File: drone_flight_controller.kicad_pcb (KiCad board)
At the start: 4 copper layers, 37 x 37 mm, 67 parts, among them J1 Conn_01x08_MountingPin, J2 USB_C_Receptacle_USB2.0_16P, U1 STM32H743VITx, U2 IST8310, U3 BMP388, U4 ICM-42688-P, U5 LT3045xDD, U6 LM5164DDA, Y1 25MHz, Y2 32.768KHz

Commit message: started placing some items
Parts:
- added H1: MountingHole, MountingHole:MountingHole_3.2mm_M3, F.Cu at (127.8, 52.8)
- added H2: MountingHole, MountingHole:MountingHole_3.2mm_M3, F.Cu at (158.2, 52.8)
- added H3: MountingHole, MountingHole:MountingHole_3.2mm_M3, F.Cu at (127.8, 83.2)
- added H4: MountingHole, MountingHole:MountingHole_3.2mm_M3, F.Cu at (158.2, 83.2)
- C10, C11, C12, C13, C14, C15, C6, C61, C62, C69, C70, C8, C9, FB1, U1, Y1, Y2: moved to B.Cu
- moved C62 87.3 mm to (151.9, 59.8), turned to -90 degrees
- moved C61 83.8 mm to (151.9, 61.6), turned to 90 degrees
- moved Y2 81.1 mm to (150.3, 60.7), turned to -90 degrees
- moved C4 74.5 mm to (201.9, 157.1)
- moved C1 74.5 mm to (217.5, 150.7)
- moved C2 74.5 mm to (216.5, 151.7)
- moved C21 74.5 mm to (247.2, 147.3)
- moved C25 74.5 mm to (206.4, 108.1)
- moved C26 74.5 mm to (206.4, 110.0)
- moved C3 74.5 mm to (214.3, 152.2)
- moved D1 74.5 mm to (202.2, 153.1)
- moved D2 74.5 mm to (202.2, 155.1)
- moved D3 74.5 mm to (247.4, 141.3)
- moved D4 74.5 mm to (247.4, 143.3)
- moved R1 74.5 mm to (199.0, 153.1)
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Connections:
- net /IMU_INT renamed /IMU_INT1
- net Net-(U2-C1) renamed /IST8310_C1
- C28 pad 1: Net-(U2-AVDD) -> +3.3V
- C29 pad 1: Net-(U2-AVDD) -> +3.3V
- U2 pad 13: Net-(U2-AVDD) -> +3.3V
- U2 pad 2: Net-(U2-AVDD) -> +3.3V
- U4 pad 9: unconnected-(U4-INT2/FSYNC/CLKIN-Pad9) -> /IMU_INT2
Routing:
- net /BUCK_SW_R: track 0.00 -> 11.0 mm, vias 0 -> 2
- net /BUCK_OUT: track 0.00 -> 7.84 mm
- net /LDO_PG: track 0.00 -> 4.15 mm, vias 0 -> 1
- net /BUCK_FB: track 0.00 -> 3.58 mm
- net /BUCK_SW: track 0.00 -> 2.79 mm
- net /LDO_IN: track 0.00 -> 2.26 mm, vias 0 -> 1
- net /BUCK_BST: track 0.00 -> 1.69 mm
- net +3.3V: track 0.00 -> 1.45 mm, vias 0 -> 3
- net /LDO_PGFB: track 0.00 -> 1.39 mm
- net /LDO_SET: track 0.00 -> 0.94 mm
- added copper zone on F.Cu, net +3.3V
- added copper zone on F.Cu, net /BUCK_OUT
- added copper zone on F.Cu, net /LDO_IN
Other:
- board size 37 x 37 mm -> 36 x 36 mm

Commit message: more placing and routing
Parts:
- R12, R13, R14, R15: moved to B.Cu
- moved R15 132.8 mm to (153.8, 69.9), turned to 90 degrees
- moved R14 132.2 mm to (153.8, 71.7), turned to 90 degrees
- moved R13 131.4 mm to (153.9, 76.2), turned to -90 degrees
- moved R12 127.5 mm to (157.8, 73.1)
- moved C1 117.1 mm to (142.4, 60.9)
- moved C2 117.1 mm to (141.4, 61.9)
- moved C3 117.1 mm to (139.2, 62.4)
- moved U4 117.1 mm to (139.7, 59.9)
- moved C4 101.4 mm to (145.8, 72.6), turned to 90 degrees
- moved D2 100.4 mm to (144.9, 72.6), turned to 90 degrees
- moved R2 99.2 mm to (144.0, 72.6), turned to 90 degrees
- moved D1 96.8 mm to (146.3, 74.0), turned to 180 degrees
- moved R1 96.1 mm to (144.4, 74.0)
- moved U3 74.1 mm to (157.6, 64.6)
- moved C26 67.4 mm to (158.4, 62.8)
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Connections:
- net Net-(J2-CC1) renamed /CC1
- net Net-(J2-CC2) renamed /CC2
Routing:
- net /MOT_1: track 0.00 -> 18.0 mm, vias 0 -> 1
- net /MOT_2: track 0.00 -> 17.4 mm, vias 0 -> 1
- net /MOT_3: track 0.00 -> 16.9 mm, vias 0 -> 1
- net /MOT_4: track 0.00 -> 15.9 mm, vias 0 -> 1
- net /VBAT_REF: track 0.00 -> 10.5 mm, vias 0 -> 1
- net /USB_VBUS: track 0.00 -> 9.03 mm
- net +3V3: track 0.00 -> 1.58 mm
- net /CC2: track 0.00 -> 1.06 mm
- net /CC1: track 0.00 -> 1.05 mm
- net /USB_VBUS_SNS: track 0.00 -> 0.86 mm
- added copper zone on F.Cu, net /VBAT_REF

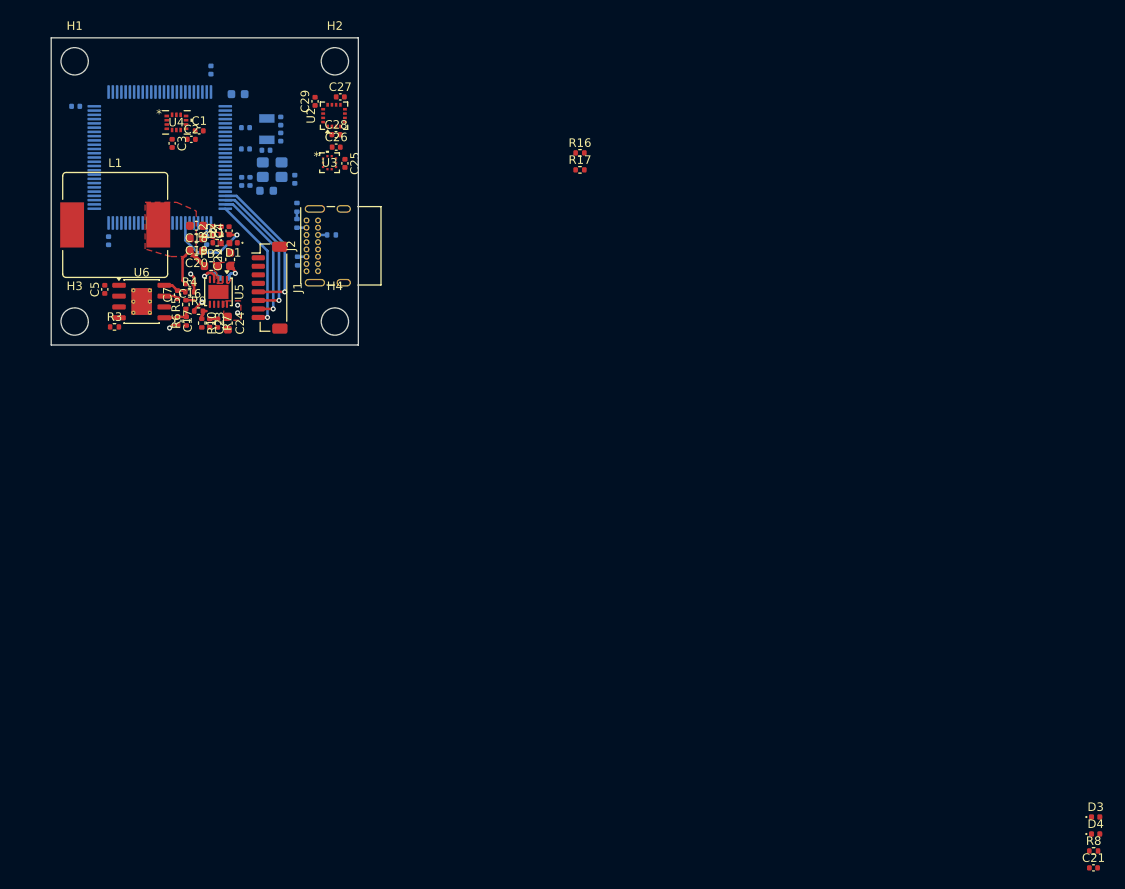
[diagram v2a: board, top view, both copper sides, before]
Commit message: added most components
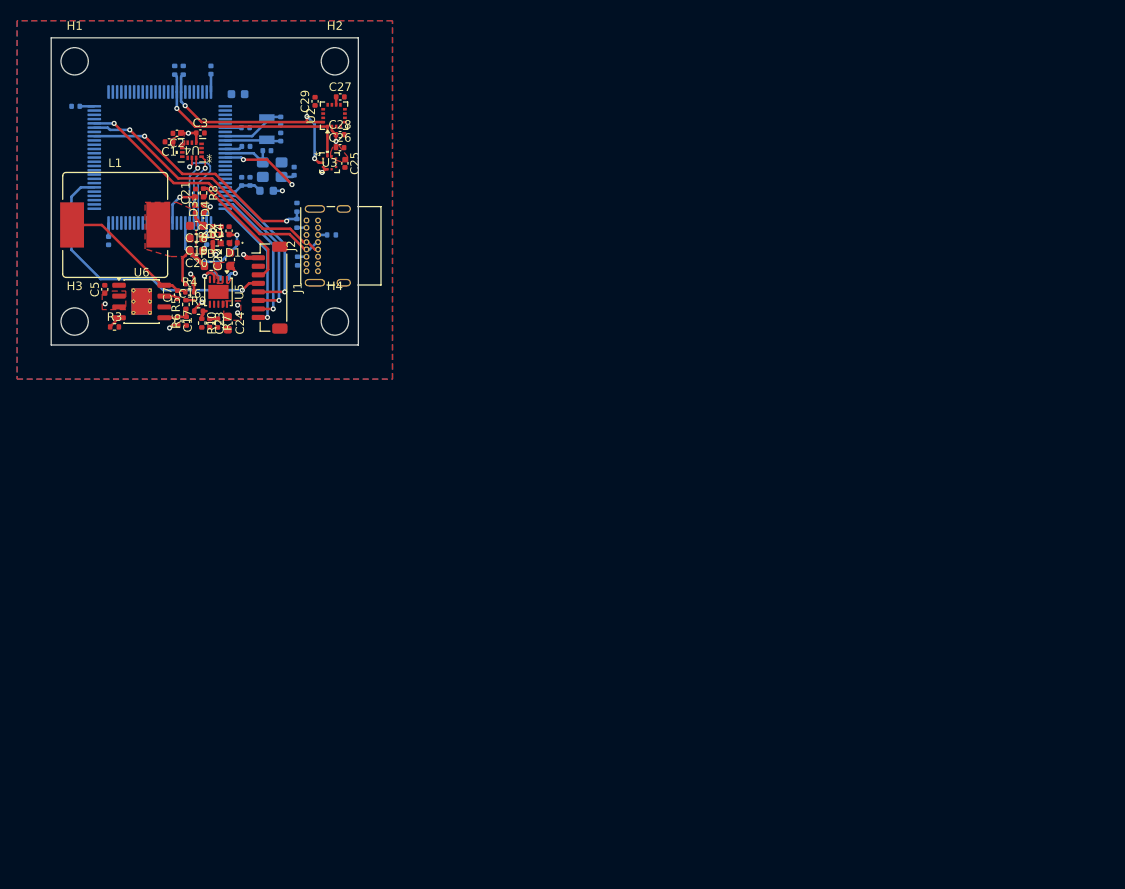
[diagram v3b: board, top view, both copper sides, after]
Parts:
- C17: value 82pF -> 56pF
- L1: value 56uH -> 33uH
- R16, R17: moved to B.Cu
- R3: value 64.9k -> 41.2k
- R4: value 422k -> 237k
- R5: value 220k -> 316k
- moved C21 131.6 mm to (141.9, 68.2), turned to 90 degrees
- moved R8 129.7 mm to (142.8, 68.2), turned to -90 degrees
- moved D4 128.5 mm to (141.9, 70.1), turned to -90 degrees
- moved D3 126.6 mm to (142.8, 70.0), turned to 90 degrees
- moved R16 48.5 mm to (139.5, 53.8), turned to -90 degrees
- moved R17 47.9 mm to (140.5, 53.8), turned to -90 degrees
- moved C69 4.68 mm to (150.3, 63.2), turned to 0 degrees
- moved C70 4.11 mm to (153.5, 65.6), turned to 90 degrees
- moved C1 3.76 mm to (138.8, 62.2), turned to 180 degrees
- moved U4 3.74 mm to (141.5, 63.2), turned to 180 degrees
- moved C3 3.52 mm to (142.5, 61.1), turned to 0 degrees
- moved C2 1.82 mm to (139.7, 61.2), turned to 180 degrees
- moved C28 0.47 mm to (158.8, 61.3)
- moved C26 0.45 mm to (158.8, 62.9)
- moved C15 0.30 mm to (147.8, 62.7)
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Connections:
- net /BUCK_OUT renamed +5V
- C10 pad 1: +3V3 -> +3.3V
- C11 pad 1: +3V3 -> +3.3V
- C12 pad 1: +3V3 -> +3.3V
- C15 pad 1: +3V3 -> +3.3V
- C6 pad 1: +3V3 -> +3.3V
- C8 pad 1: +3V3 -> +3.3V
- C9 pad 1: +3V3 -> +3.3V
- FB1 pad 2: +3V3 -> +3.3V
- U1 pad 100: +3V3 -> +3.3V
- U1 pad 11: +3V3 -> +3.3V
- U1 pad 27: +3V3 -> +3.3V
- U1 pad 28: /SPI_CS -> unconnected-(U1-PA4-Pad28)
- U1 pad 50: +3V3 -> +3.3V
- U1 pad 6: +3V3 -> +3.3V
- U1 pad 75: +3V3 -> +3.3V
- U1 pad 92: unconnected-(U1-PB6-Pad92) -> /I2C_SCL
- U1 pad 93: unconnected-(U1-PB7-Pad93) -> /I2C_SDA
- U4 pad 12: /SPI_CS -> /IMU_CS
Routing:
- net /ESC_TELEM: track 0.00 -> 33.5 mm, vias 0 -> 1
- net /USB_DP: track 0.00 -> 32.7 mm, vias 0 -> 1
- net /USB_DM: track 0.00 -> 32.1 mm, vias 0 -> 1
- net /I2C_SDA: track 0.00 -> 28.1 mm, vias 0 -> 3
- net /USB_VBUS_SNS: track 0.86 -> 28.8 mm, vias 0 -> 2
- net /I2C_SCL: track 0.00 -> 26.1 mm, vias 0 -> 1
- net +BATT: track 0.00 -> 22.0 mm, vias 0 -> 3
- net +3.3V: track 1.45 -> 23.4 mm, vias 3 -> 8
- net /ESC_CS: track 0.00 -> 14.3 mm
- net /BUCK_SW: track 2.79 -> 16.5 mm
- net /HSE_OUT: track 0.00 -> 12.3 mm, vias 0 -> 2
- net /SPI_CLK: track 0.00 -> 11.2 mm, vias 0 -> 1
- net /SPI_MISO: track 0.00 -> 8.50 mm, vias 0 -> 1
- net /SPI_MOSI: track 0.00 -> 8.10 mm, vias 0 -> 1
- net /LSE_IN: track 0.00 -> 7.64 mm
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- added copper zone on In2.Cu, net +3.3V
- added copper zone on F.Cu, net +BATT
- added copper zone on F.Cu, net /CS_REF
- added copper zone on B.Cu, net GND
- added copper zone on F.Cu, net GND
- added copper zone on In1.Cu, net GND

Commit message: routing + final commit before reducing size
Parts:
- added J3: Conn_01x06_MountingPin, Connector_JST:JST_SH_BM06B-SRSS-TB_1x06-1MP_P1.00mm_Vertical, F.Cu at (141.4, 54.9)
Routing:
- net +5V: track 7.84 -> 63.4 mm, vias 0 -> 2
- net /I2C_SCL: track 26.1 -> 31.2 mm
- net /I2C_SDA: track 28.1 -> 32.8 mm

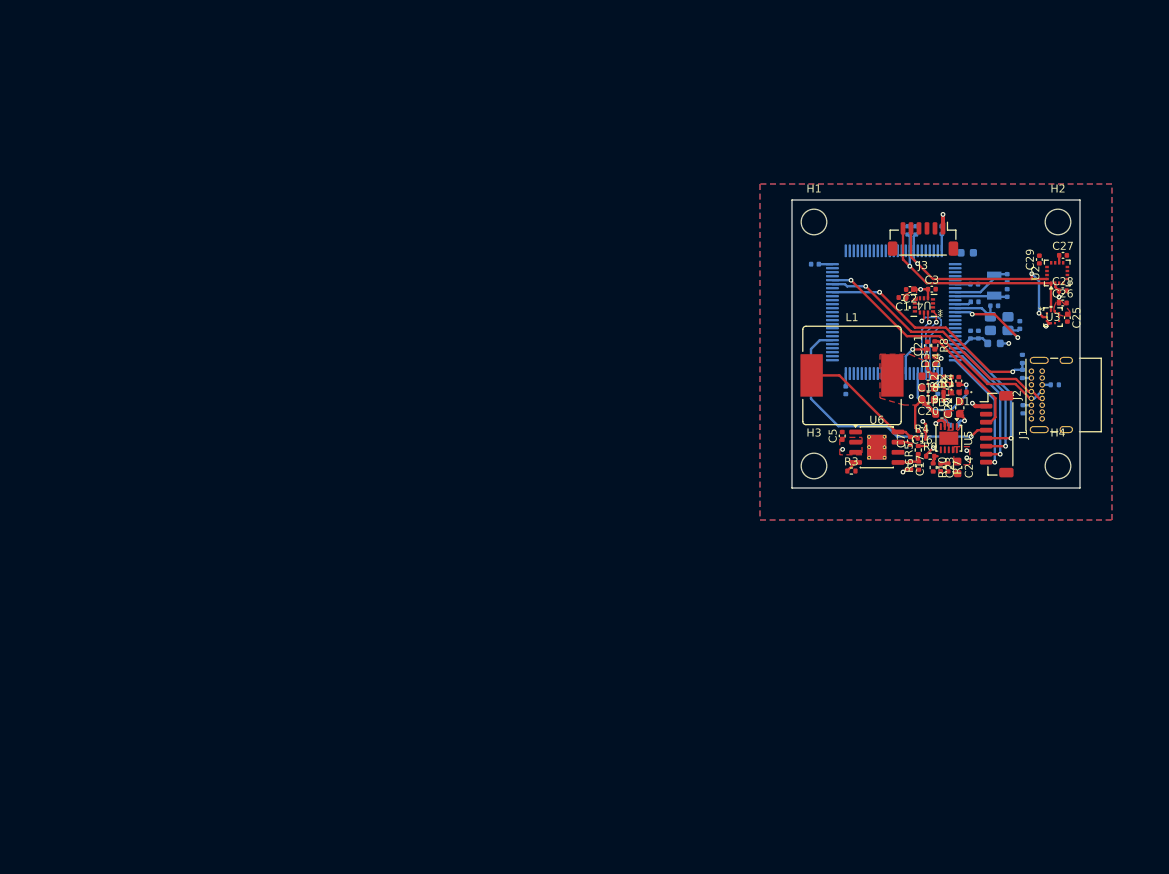
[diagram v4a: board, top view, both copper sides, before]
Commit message: started downsizing to 25.5mm
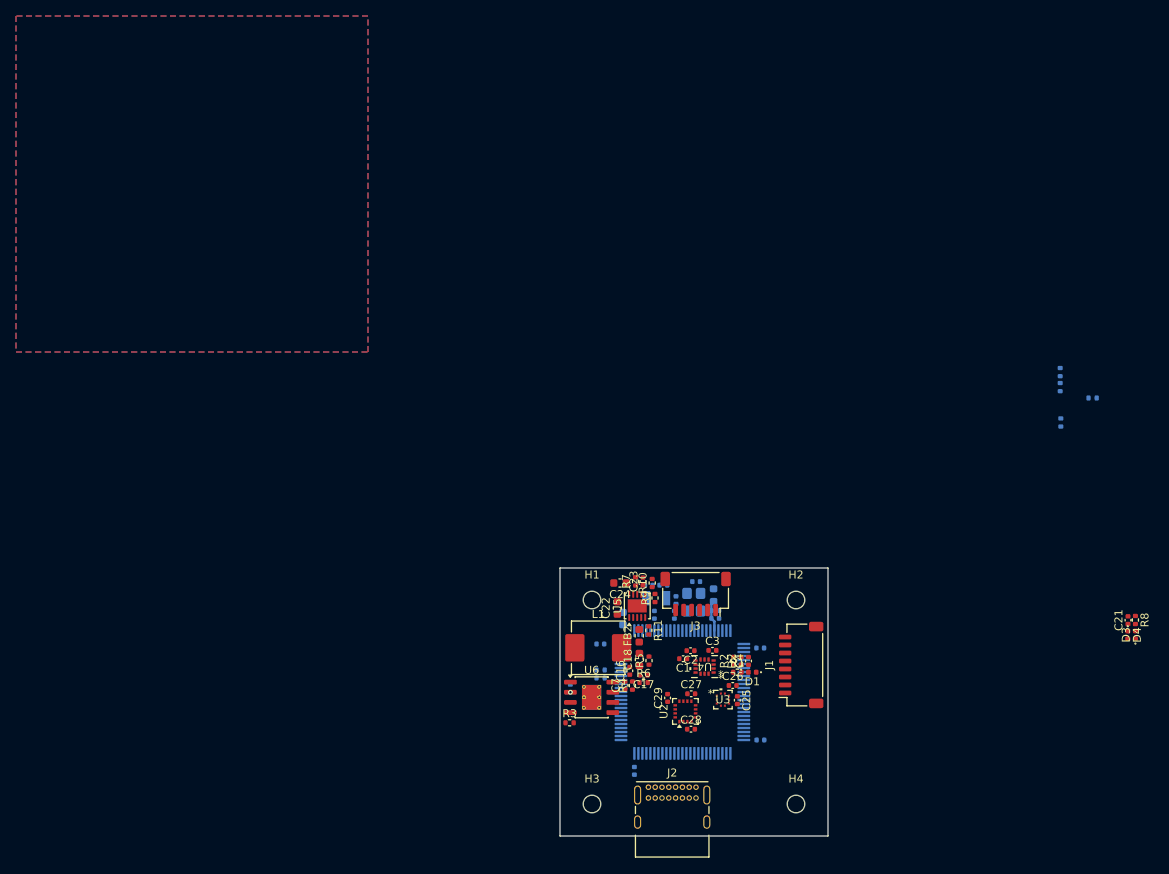
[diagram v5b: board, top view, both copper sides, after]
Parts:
- removed C19, C20: 22uF, Capacitor_SMD:C_0603_1608Metric
- C5: moved to B.Cu
- H1, H2, H3, H4: footprint MountingHole:MountingHole_3.2mm_M3 -> MountingHole:MountingHole_2.2mm_M2
- J1: footprint Connector_JST:JST_SH_BM08B-SRSS-TB_1x08-1MP_P1.00mm_Vertical -> Connector_JST:JST_SH_SM08B-SRSS-TB_1x08-1MP_P1.00mm_Horizontal
- J3: footprint Connector_JST:JST_SH_BM06B-SRSS-TB_1x06-1MP_P1.00mm_Vertical -> Connector_JST:JST_SH_SM06B-SRSS-TB_1x06-1MP_P1.00mm_Horizontal
- L1: footprint Inductor_SMD:L_Bourns_SRR1210A -> Inductor_SMD:L_Vishay_IHLP-2525
- R11: moved to F.Cu
- moved C29 71.9 mm to (109.5, 112.2)
- moved U2 71.9 mm to (111.7, 113.9)
- moved C27 71.9 mm to (112.4, 111.7)
- moved C28 71.9 mm to (112.4, 116.1)
- moved R16 67.9 mm to (101.1, 109.8), turned to 0 degrees
- moved R17 67.6 mm to (101.1, 108.8), turned to 0 degrees
- moved C8 67.2 mm to (105.3, 121.4), turned to -90 degrees
- moved C6 67.1 mm to (101.0, 105.5), turned to 180 degrees
- moved J2 66.4 mm to (107.0, 123.4), turned to 0 degrees
- moved C25 63.2 mm to (118.2, 112.5)
- moved C26 63.2 mm to (117.6, 110.7)
- moved U3 63.2 mm to (116.4, 112.5)
- moved C12 62.8 mm to (103.9, 102.3), turned to 90 degrees
- moved C62 59.0 mm to (107.1, 98.2), turned to 0 degrees
- moved Y2 57.5 mm to (108.0, 99.8), turned to 0 degrees
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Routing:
- net +5V: track 63.4 -> 0.00 mm, vias 2 -> 0
- net /ESC_TELEM: track 33.5 -> 0.00 mm, vias 1 -> 0
- net /I2C_SDA: track 32.8 -> 0.00 mm, vias 3 -> 0
- net /USB_DP: track 32.7 -> 0.00 mm, vias 1 -> 0
- net /USB_DM: track 32.1 -> 0.00 mm, vias 1 -> 0
- net /I2C_SCL: track 31.2 -> 0.00 mm, vias 1 -> 0
- net /USB_VBUS_SNS: track 28.8 -> 0.00 mm, vias 2 -> 0
- net +3.3V: track 23.4 -> 0.00 mm, vias 8 -> 0
- net +BATT: track 22.0 -> 0.00 mm, vias 3 -> 1
- net /MOT_1: track 18.0 -> 0.00 mm, vias 1 -> 0
- net /MOT_2: track 17.4 -> 0.00 mm, vias 1 -> 0
- net /MOT_3: track 16.9 -> 0.00 mm, vias 1 -> 0
- net /BUCK_SW: track 16.5 -> 0.00 mm
- net /MOT_4: track 15.9 -> 0.00 mm, vias 1 -> 0
- net /ESC_CS: track 14.3 -> 0.00 mm
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- removed copper zone on F.Cu, net +3.3V
- removed copper zone on F.Cu, net +5V
- removed copper zone on F.Cu, net +BATT
- removed copper zone on F.Cu, net /CS_REF
- removed copper zone on F.Cu, net /LDO_IN
- removed copper zone on F.Cu, net /VBAT_REF
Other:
- board size 36 x 36 mm -> 33.5 x 33.5 mm
